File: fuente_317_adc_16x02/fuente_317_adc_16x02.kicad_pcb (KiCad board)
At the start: 2 copper layers, 100 x 100 mm, 78 parts, among them J1 Fuente, J10 3V3, J11 GND, J12 +12V, J13 -12V, J14 +1.2V, J15 -1.2V, J16 -5V, J17 Vadj+, J18 Vadj-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

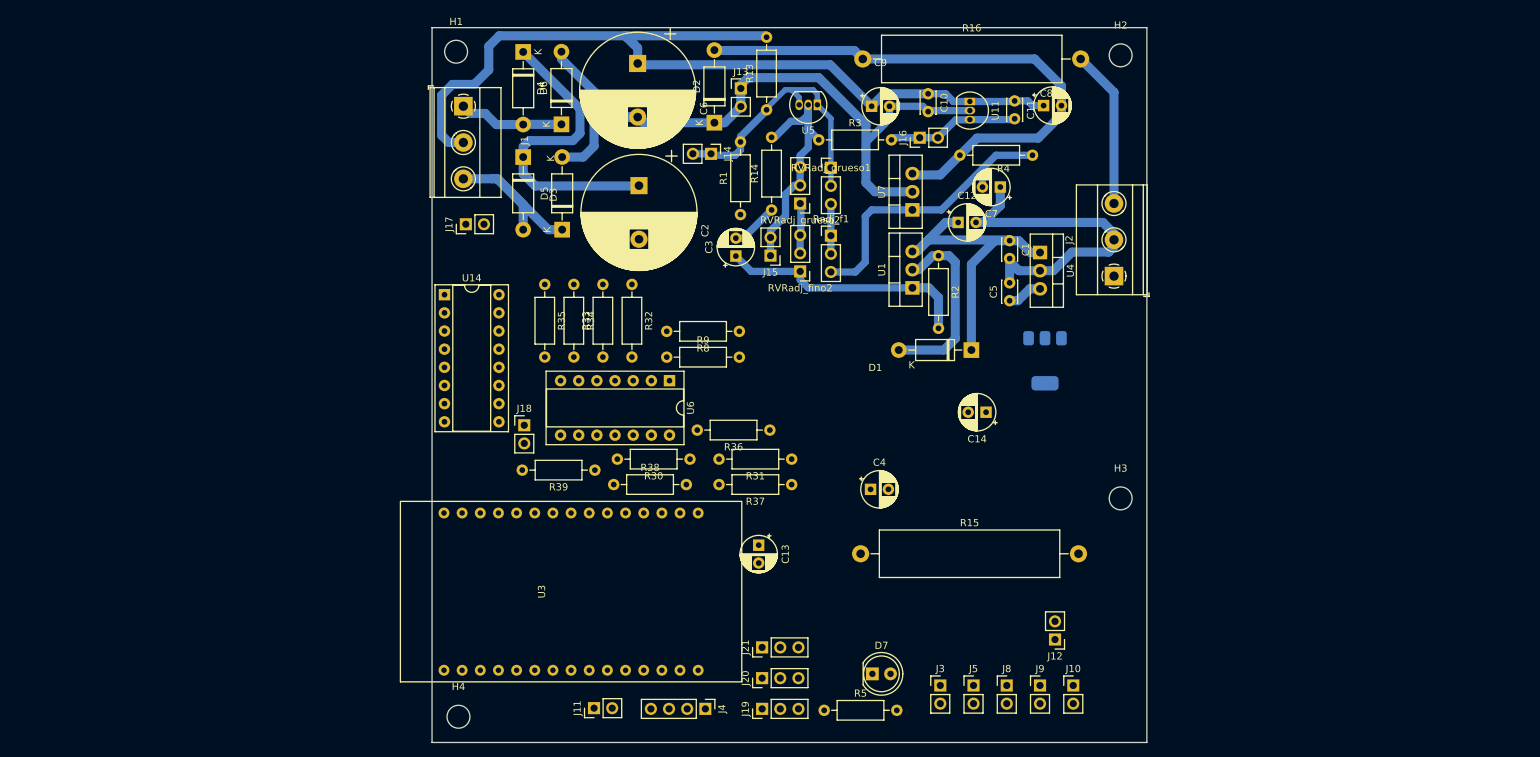
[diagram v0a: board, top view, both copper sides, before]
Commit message: fuente_317_337: start to wire OP AMP
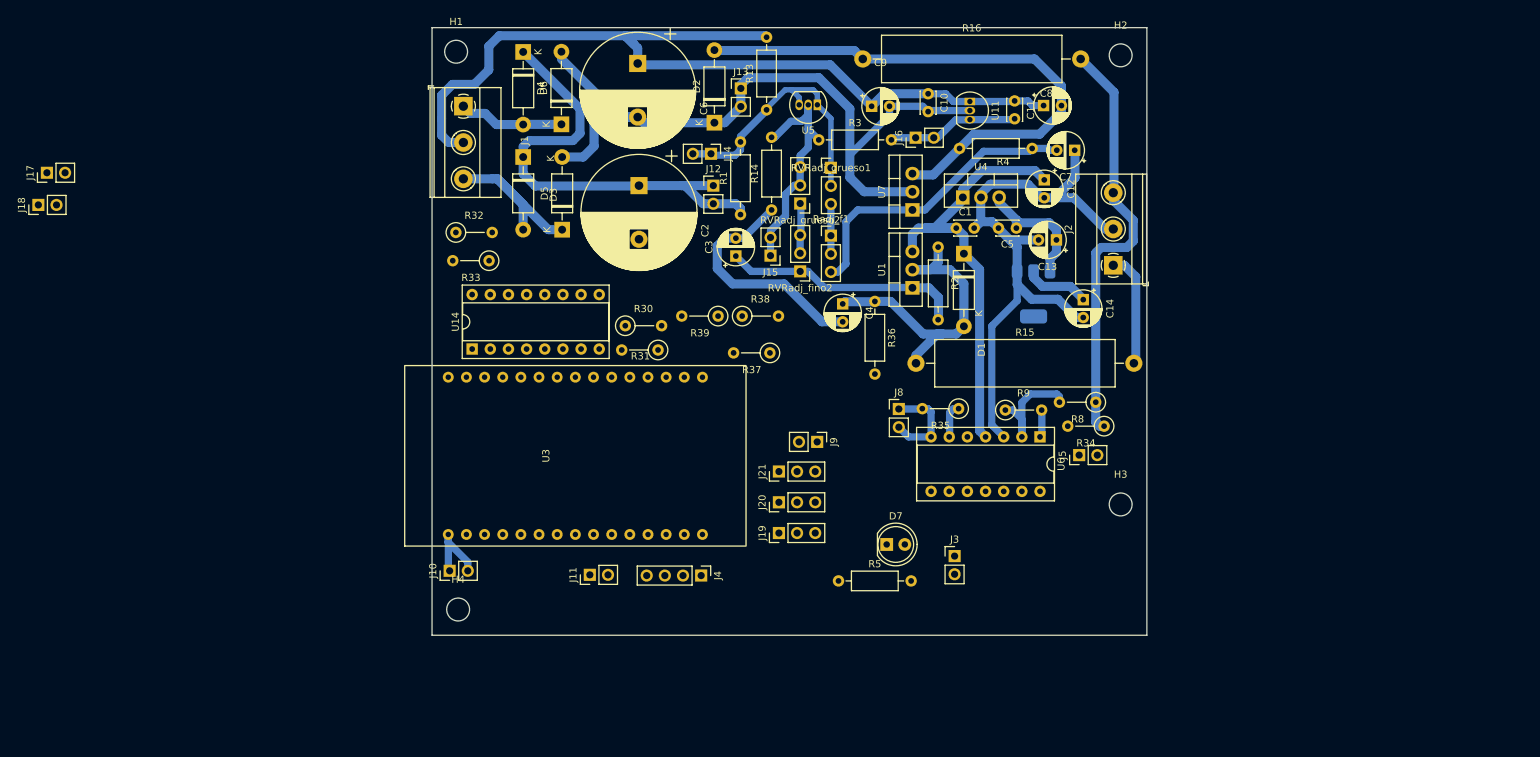
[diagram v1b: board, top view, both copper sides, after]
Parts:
- R1: value 47k -> 22k
- R3: value 47k -> 6k8
- R30, R31, R32, R33, R34, R35, R37, R38, R39, R8, R9: footprint Resistor_THT:R_Axial_DIN0207_L6.3mm_D2.5mm_P10.16mm_Horizontal -> Resistor_THT:R_Axial_DIN0207_L6.3mm_D2.5mm_P5.08mm_Vertical
- moved J10 88.7 mm to (22.5, 96.0), turned to 90 degrees
- moved J12 79.5 mm to (59.4, 42.1), turned to 0 degrees
- moved R34 76.8 mm to (114.0, 75.8), turned to 180 degrees
- moved J18 74.6 mm to (-35.1, 44.8), turned to 90 degrees
- moved R35 60.4 mm to (93.7, 73.3), turned to 180 degrees
- moved C13 59.6 mm to (107.3, 49.7), turned to 180 degrees
- moved J17 59.0 mm to (-33.9, 40.3)
- moved U6 52.4 mm to (105.0, 77.2)
- moved R8 50.8 mm to (112.8, 72.4)
- moved R9 47.9 mm to (100.2, 73.5)
- moved J9 46.2 mm to (73.9, 78.0), turned to -90 degrees
- moved J8 41.5 mm to (85.3, 73.3)
- moved J5 35.5 mm to (110.5, 79.8), turned to 90 degrees
- moved R38 29.6 mm to (63.4, 60.4)
- moved R15 27.8 mm to (87.7, 67.0)
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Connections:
- R1 pad 1: +5V -> +12V
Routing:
- net GND: track 183.1 -> 249.4 mm
- net +12V: track 90.2 -> 130.7 mm
- net Vout-: track 22.1 -> 59.6 mm
- net +3V3: track 0.00 -> 20.5 mm
- net Io1+: track 26.5 -> 45.6 mm
- net Net-(U6A--): track 0.00 -> 16.8 mm
- net Vout+: track 0.00 -> 16.0 mm
- net Iadc-: track 0.00 -> 13.3 mm
- net +5V: track 4.94 -> 17.7 mm
- net Net-(U6B--): track 0.00 -> 4.91 mm
- net Vadc-: track 0.00 -> 3.86 mm
- net -12V: track 102.6 -> 105.7 mm
- net Net-(U1-ADJ): track 35.7 -> 33.9 mm
- net Net-(U7-ADJ): track 41.3 -> 42.3 mm
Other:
- board size 100 x 100 mm -> 100 x 85 mm

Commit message: Change position of LM7805 and 3v3
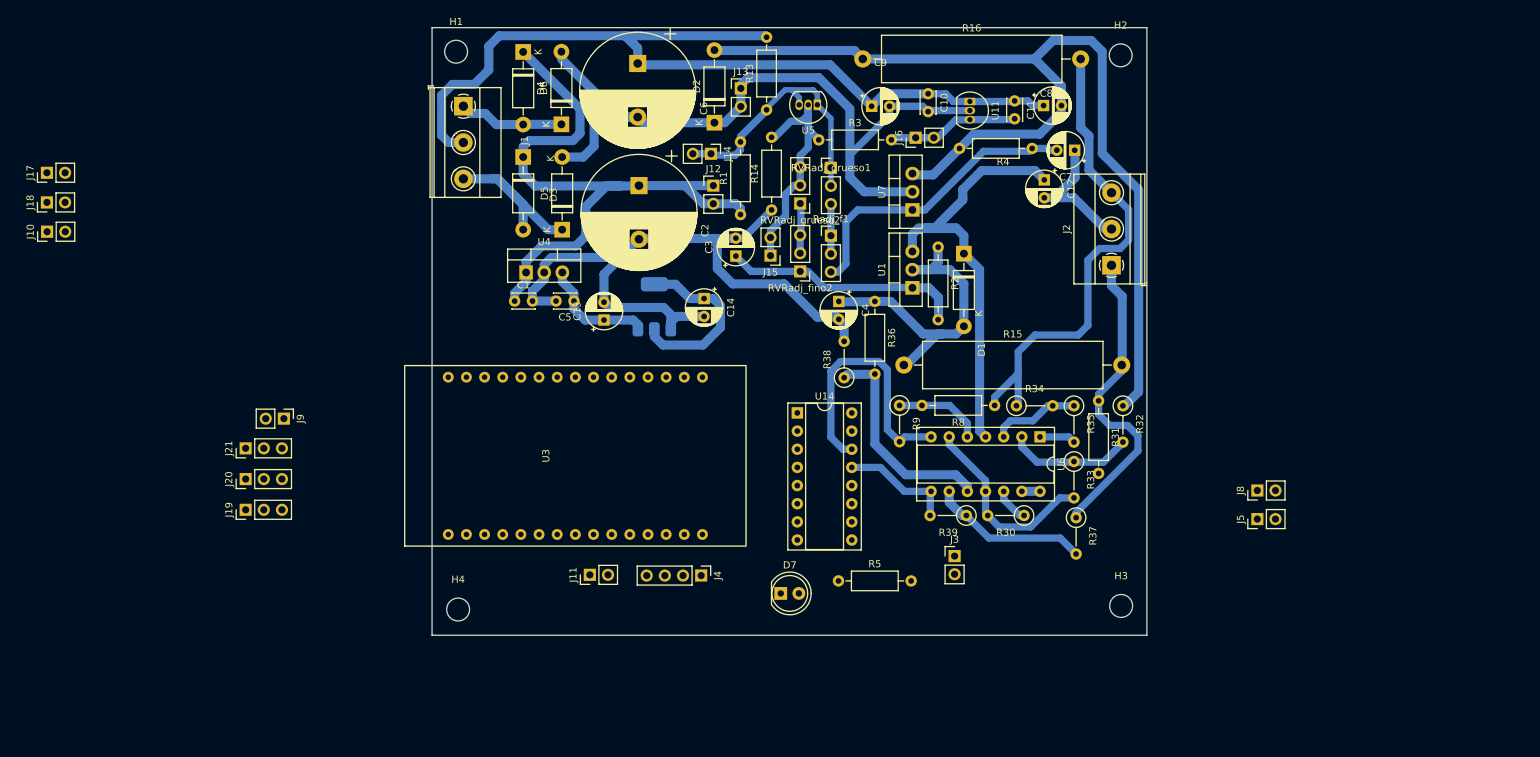
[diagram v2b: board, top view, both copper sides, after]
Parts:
- R31, R8: footprint Resistor_THT:R_Axial_DIN0207_L6.3mm_D2.5mm_P5.08mm_Vertical -> Resistor_THT:R_Axial_DIN0207_L6.3mm_D2.5mm_P10.16mm_Horizontal
- R33, R38: value 47k -> 10k
- moved R32 96.4 mm to (116.7, 72.9), turned to -90 degrees
- moved R33 86.5 mm to (109.8, 80.7), turned to -90 degrees
- moved J19 74.7 mm to (-6.08, 87.5)
- moved J20 74.7 mm to (-6.08, 83.2)
- moved J21 74.7 mm to (-6.08, 78.8)
- moved J9 74.7 mm to (-0.72, 74.7)
- moved J10 73.6 mm to (-33.9, 48.5)
- moved C13 64.3 mm to (44.1, 60.9), turned to 90 degrees
- moved C5 62.7 mm to (39.9, 58.2)
- moved C1 62.6 mm to (31.6, 58.2)
- moved R31 62.0 mm to (113.2, 72.2), turned to -90 degrees
- moved U4 62.0 mm to (33.1, 54.2)
- moved R30 61.8 mm to (102.8, 88.2), turned to 180 degrees
- moved U13 53.1 mm to (51.1, 59.0), turned to 90 degrees
- moved C14 53.0 mm to (58.1, 57.9)
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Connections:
- R32 pad 2: Net-(U6B-+) -> Net-(U6A--)
- R33 pad 1: Net-(U6B-+) -> Net-(U6A--)
- R34 pad 2: Net-(U6B--) -> Net-(U6A-+)
- R35 pad 1: Net-(U6B--) -> Net-(U6A-+)
- R8 pad 2: Net-(U6A--) -> Net-(U6B-+)
- R9 pad 1: Net-(U6A--) -> Net-(U6B-+)
- U6 pad 1: Vadc- -> Iadc-
- U6 pad 3: GND -> Net-(U6A-+)
- U6 pad 6: Net-(U6B--) -> GND
- U6 pad 7: Iadc- -> Vadc-
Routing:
- net Io1-: track 78.9 -> 142.8 mm
- net Vadc-: track 3.86 -> 37.3 mm
- net Net-(U6C-+): track 0.00 -> 30.4 mm
- net Vout+: track 16.0 -> 44.6 mm
- net +12V: track 130.7 -> 156.9 mm
- net GND: track 249.4 -> 273.3 mm
- net Net-(U6C--): track 0.00 -> 22.3 mm
- net Iadc+: track 0.00 -> 15.9 mm
- net Net-(U6B-+): track 0.00 -> 12.4 mm
- net Net-(U6A-+): track 0.00 -> 12.4 mm
- net Vout-: track 59.6 -> 68.8 mm
- net Iadc-: track 13.3 -> 5.05 mm
- net Net-(U6D-+): track 0.00 -> 4.92 mm
- net Net-(U6B--): track 4.91 -> 0.00 mm
- net +3V3: track 20.5 -> 25.3 mm
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
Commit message: fuente_317_337: pcb finalizado de fuente y controlador
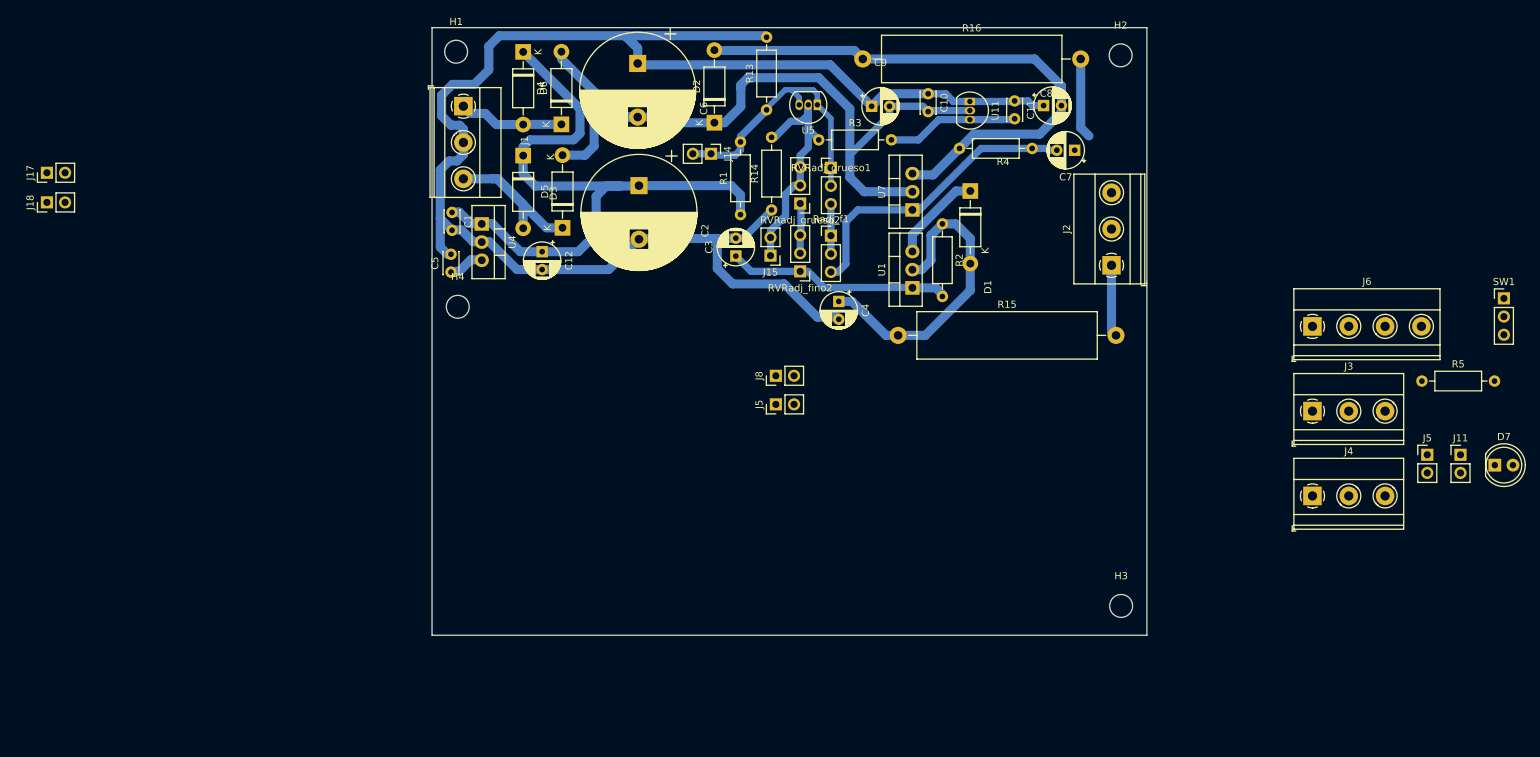
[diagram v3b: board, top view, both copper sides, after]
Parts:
- removed C13, C14: 10uF, Capacitor_THT:CP_Radial_D5.0mm_P2.50mm
- removed J10: 3V3, Connector_PinHeader_2.54mm:PinHeader_1x02_P2.54mm_Vertical
- removed J12: +12V, Connector_PinHeader_2.54mm:PinHeader_1x02_P2.54mm_Vertical
- removed J13: -12V, Connector_PinHeader_2.54mm:PinHeader_1x02_P2.54mm_Vertical
- removed J16: -5V, Connector_PinHeader_2.54mm:PinHeader_1x02_P2.54mm_Vertical
- removed J19: BTN_POWER, Connector_PinHeader_2.54mm:PinHeader_1x03_P2.54mm_Vertical
- removed J20: BTN_MODE, Connector_PinHeader_2.54mm:PinHeader_1x03_P2.54mm_Vertical
- removed J21: BTN_SEL, Connector_PinHeader_2.54mm:PinHeader_1x03_P2.54mm_Vertical
- removed J9: 5V, Connector_PinHeader_2.54mm:PinHeader_1x02_P2.54mm_Vertical
- removed R30: 47k, Resistor_THT:R_Axial_DIN0207_L6.3mm_D2.5mm_P5.08mm_Vertical
- removed R31, R36, R8: 10k, Resistor_THT:R_Axial_DIN0207_L6.3mm_D2.5mm_P10.16mm_Horizontal
- removed R32, R33, R34, R35, R37, R38, R39, R9: 10k, Resistor_THT:R_Axial_DIN0207_L6.3mm_D2.5mm_P5.08mm_Vertical
- removed U13: AMS1117-3.3, Package_TO_SOT_SMD:SOT-223-3_TabPin2
- removed U14: CD4051B, Package_DIP:CERDIP-16_W7.62mm_SideBrazed_Socket
- removed U3: ~, Componentes_Proyecto_Digitales:Esp-8266-DevKit
- removed U6: LM324, Package_DIP:CERDIP-14_W7.62mm_SideBrazed_Socket
- added J5: Cooler, Connector_PinHeader_2.54mm:PinHeader_1x02_P2.54mm_Vertical, F.Cu at (159.2, 79.8)
- added J6: Inputs, TerminalBlock_Phoenix:TerminalBlock_Phoenix_MKDS-1,5-4-5.08_1x04_P5.08mm_Horizontal, F.Cu at (143.2, 61.8)
- added SW1: SW_SPDT, Connector_PinHeader_2.54mm:PinHeader_1x03_P2.54mm_Vertical, F.Cu at (169.9, 57.9)
- J3: value UART -> Salida_5v; footprint Connector_PinHeader_2.54mm:PinHeader_1x02_P2.54mm_Vertical -> TerminalBlock_Phoenix:TerminalBlock_Phoenix_MKDS-1,5-3-5.08_1x03_P5.08mm_Horizontal
- J4: value LCD16x2 -> Salida_12v; footprint Connector_PinHeader_2.54mm:PinHeader_1x04_P2.54mm_Vertical -> TerminalBlock_Phoenix:TerminalBlock_Phoenix_MKDS-1,5-3-5.08_1x03_P5.08mm_Horizontal
- R3: value 6k8 -> 22k
- R5: value 120 -> 200
- moved J11 123.0 mm to (163.9, 79.8), turned to 0 degrees
- moved D7 101.5 mm to (168.7, 81.2)
- moved R5 86.3 mm to (158.5, 69.4)
- moved J4 86.2 mm to (143.2, 85.5), turned to 0 degrees
- moved C12 71.0 mm to (35.4, 51.3)
- moved J5 69.2 mm to (68.1, 72.7)
- moved J8 69.2 mm to (68.1, 68.7)
- moved J3 54.0 mm to (143.2, 73.7)
- moved H4 42.4 mm to (23.6, 59.0)
- moved C5 17.7 mm to (22.6, 54.2), turned to 90 degrees
- moved C1 15.2 mm to (22.8, 45.9), turned to -90 degrees
- moved U4 9.19 mm to (27.0, 47.5), turned to -90 degrees
- moved D1 8.82 mm to (95.3, 42.9)
- moved R15 4.23 mm to (85.2, 63.0)
- moved R2 3.30 mm to (91.4, 47.5)
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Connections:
- J3 pad 1: RX_esp -> +5V
- J3 pad 2: TX_esp -> GND
- J4 pad 1: +5V -> +12V
- J4 pad 2: I2C - SCL -> GND
- J4 pad 3: I2C - SDA -> -12V
- R1 pad 1: +12V -> +5V
- R5 pad 1: +3V3 -> +5V
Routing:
- net Io1-: track 142.8 -> 78.9 mm
- net Vout-: track 68.8 -> 11.2 mm
- net +12V: track 156.9 -> 107.5 mm
- net GND: track 273.3 -> 224.5 mm
- net Vadc-: track 37.3 -> 0.00 mm
- net Vout+: track 44.6 -> 10.1 mm
- net Net-(U6C-+): track 30.4 -> 0.00 mm
- net +3V3: track 25.3 -> 0.00 mm
- net Net-(U6C--): track 22.3 -> 0.00 mm
- net Net-(U6A--): track 17.7 -> 0.00 mm
- net Iadc+: track 15.9 -> 0.00 mm
- net Net-(U6B-+): track 12.4 -> 0.00 mm
- net Net-(U6A-+): track 12.4 -> 0.00 mm
- net +5V: track 16.3 -> 4.67 mm
- net Iadc-: track 5.05 -> 0.00 mm
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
